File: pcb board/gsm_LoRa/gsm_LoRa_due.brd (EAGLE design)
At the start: 71.4 x 51.2 mm, 37 parts, among them IC1 TPS22810TDBVRQ1, IC3 DS3231MZ+, X1 22-23-2021

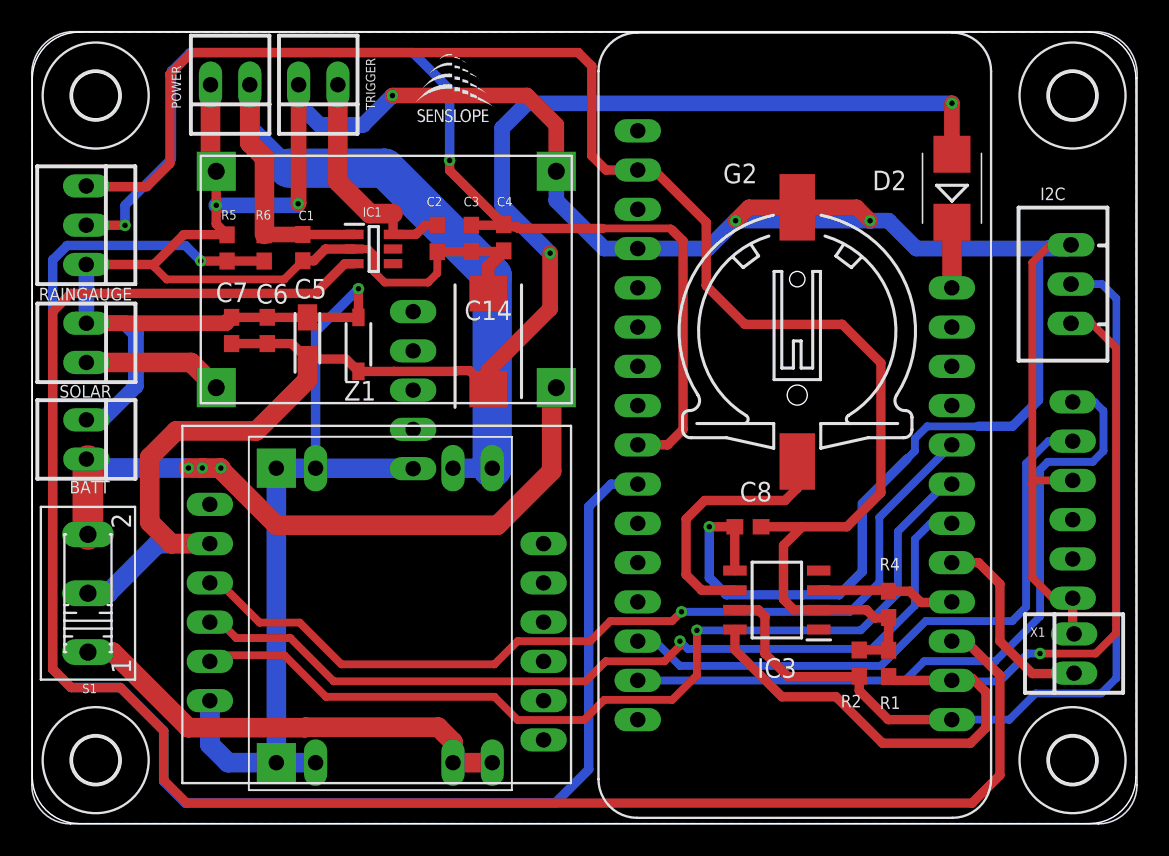
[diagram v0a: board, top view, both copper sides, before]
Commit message: added SPI connector
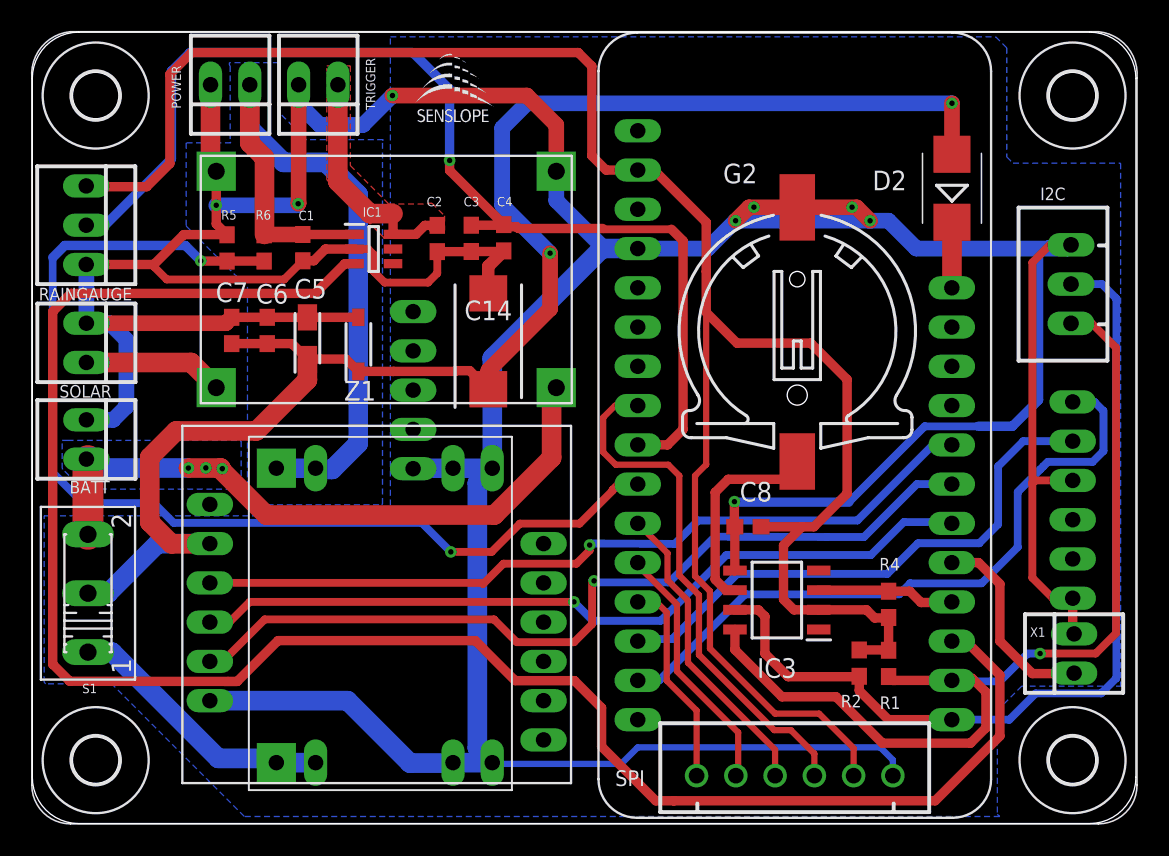
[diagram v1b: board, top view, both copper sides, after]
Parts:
- added SPI: JST-XH-06-PIN-ROUND-PAD, Rembrandt Electronics - JST XH Connectors v1-0:JST-XH-06-PACKAGE-ROUND-PAD
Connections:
- new net CS: SPI.4, U$1.P$8
- new net MISO: SPI.1, U$1.P$13
- new net MOSI: SPI.2, U$1.P$12
- new net SCK: SPI.3, U$1.P$11
- net +3V3: now also SPI.5
- net 12VIN: now also U$10.+IN, U$10.+IN1; no longer U$10.-IN, U$10.-IN1
- net DC-DC: now also U$10.+OUT, U$10.+OUT1; no longer U$10.-OUT, U$10.-OUT1
- net GND: now also SPI.6, U$10.-IN, U$10.-IN1, U$10.-OUT, U$10.-OUT1; no longer U$10.+IN, U$10.+IN1, U$10.+OUT, U$10.+OUT1
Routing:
- net +3V3: track 106.1 -> 141.0 mm
- net CS: track 0.00 -> 34.0 mm
- net N$5: track 102.8 -> 70.2 mm, vias 1 -> 2
- net GND: track 300.3 -> 328.2 mm, vias 7 -> 8
- net SCK: track 0.00 -> 20.0 mm
- net MOSI: track 0.00 -> 16.5 mm
- net MISO: track 0.00 -> 13.5 mm
- net DC-DC: track 29.9 -> 17.7 mm
- net GSM_RST: track 58.5 -> 52.0 mm
- net TXD_GSM: track 56.9 -> 51.7 mm
- net RX1: track 40.3 -> 35.7 mm
- net RXD_GSM: track 60.3 -> 55.7 mm
- net 12VIN: track 53.4 -> 49.7 mm
- net TX1: track 46.7 -> 43.2 mm
- net N$2: track 16.9 -> 14.0 mm
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- added copper zone on layer 16, net 12VIN
- added copper zone on layer 16, net BATT
- added copper zone on layer 1, net N$8

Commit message: Updated names on traces
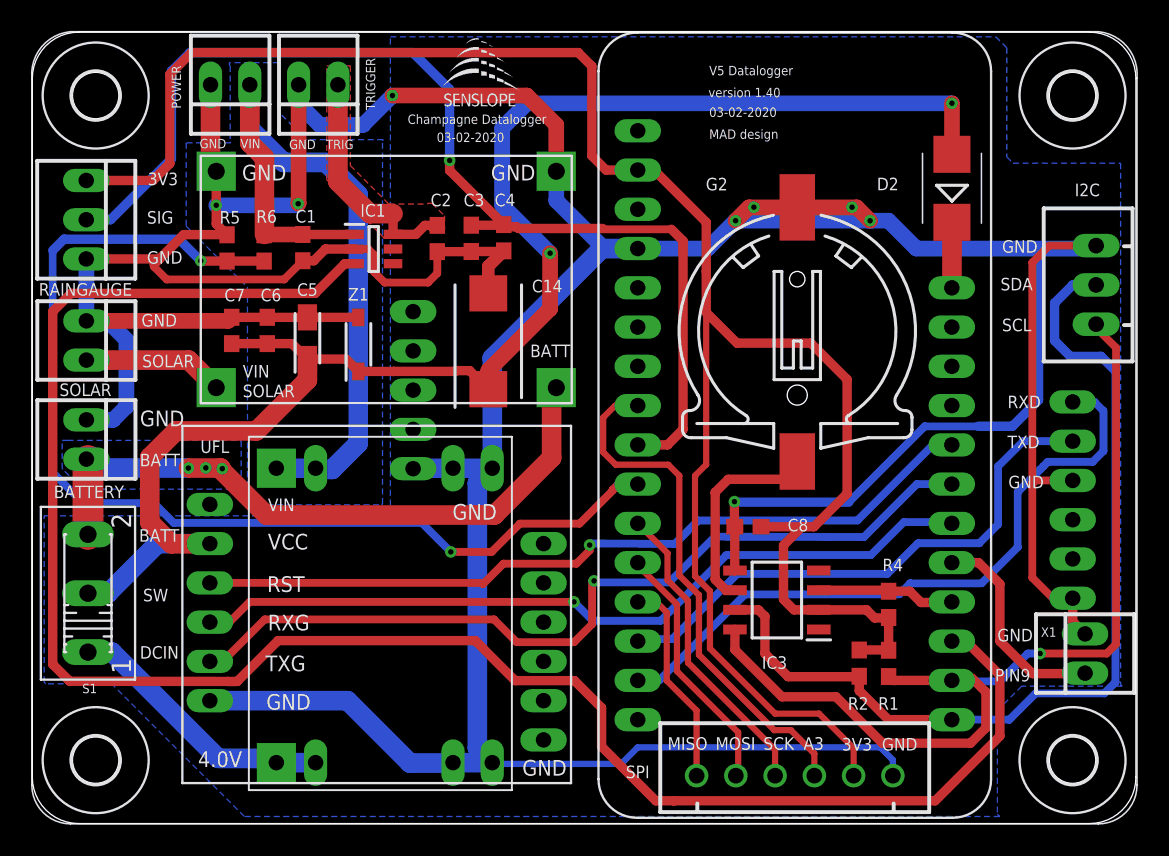
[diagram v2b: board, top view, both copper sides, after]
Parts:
- moved U$13 2.00 mm to (28.8, 47.9)
- moved I2C 1.63 mm to (68.8, 34.7)
- moved X1 0.71 mm to (68.1, 10.9)
- moved RAINGAUGE 0.36 mm to (3.49, 39.0)
- moved SOLAR 0.15 mm to (3.50, 31.2)
- renumbered BATT to BATTERY
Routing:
- net GND: track 328.2 -> 336.9 mm
- net SDA: track 58.6 -> 61.0 mm
- net SCL: track 63.6 -> 62.6 mm
- net PIN9: track 13.1 -> 13.8 mm
- net N$5: track 70.2 -> 70.8 mm
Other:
- board text added: "03-02-2020"
- board text added: "3V3"
- board text added: "4.0V"
- board text added: "A3"
- board text added: "BATT"
- board text added: "Champagne Datalogger"
- board text added: "DCIN"
- board text added: "GND"
- board text added: "MAD design"
- board text added: "MISO"
- board text added: "MOSI"
- board text added: "PIN9"
- board text added: "RST"
- board text added: "RXD"
- board text added: "RXG"
- board text added: "SCK"
- board text added: "SCL"
- board text added: "SDA"
- board text added: "SIG"
- board text added: "SOLAR"
- board text added: "SW"
- board text added: "TRIG"
- board text added: "TXD"
- board text added: "TXG"
- board text added: "UFL"
- board text added: "V5 Datalogger"
- board text added: "VCC"
- board text added: "VIN"
- board text added: "version 1.40"

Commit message: Added power IC switch for GSM Updated names of components
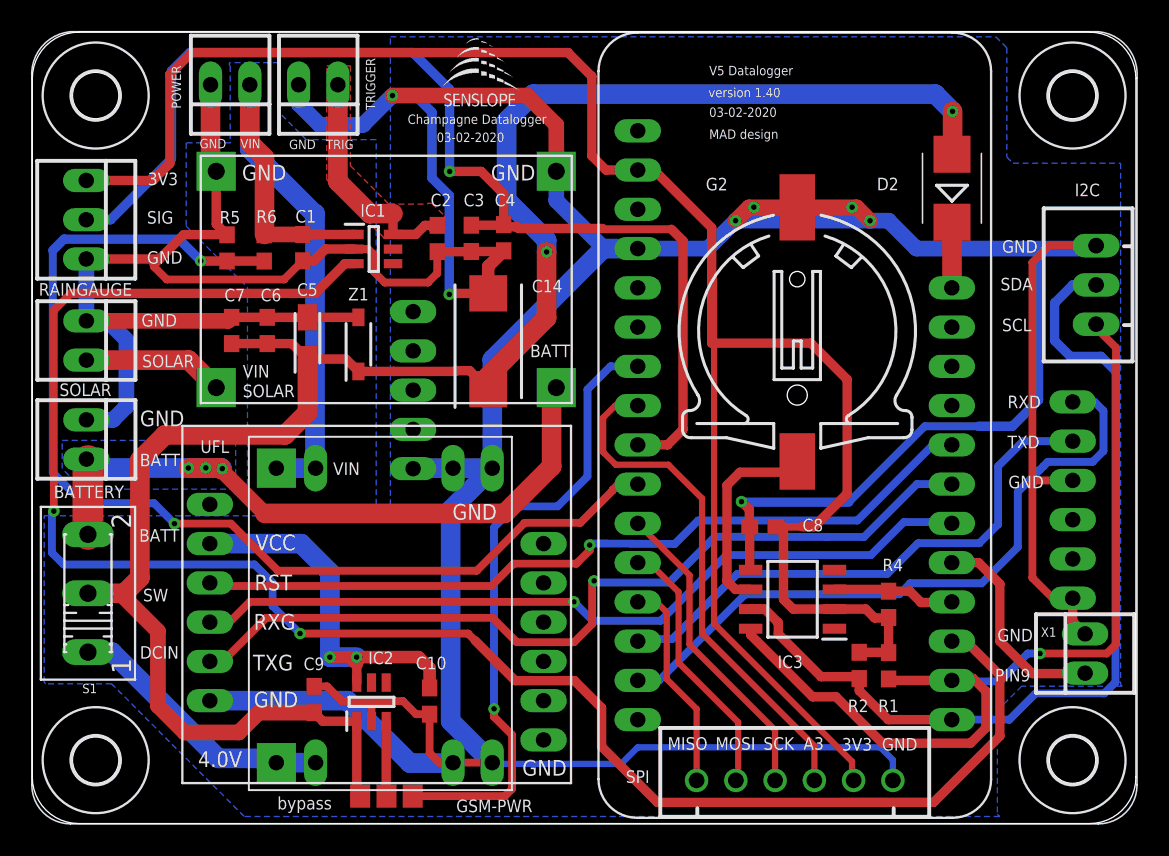
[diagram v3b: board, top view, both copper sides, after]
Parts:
- added C10, C9: (no value), eagle-ltspice:C0603
- added GSM-PWR: 0R-JUMPB, jump-0r-smd:B0R-JMP
- added IC2: TPS22810TDBVRQ1, TPS22810TDBVRQ1:SOT95P280X145-6N
- moved IC3 1.02 mm to (49.2, 14.4)
- moved C8 0.97 mm to (47.3, 19.1)
- moved SPI 0.30 mm to (49.3, 2.69)
- moved R1 0.15 mm to (55.4, 10.1)
- moved R2 0.15 mm to (53.5, 10.1)
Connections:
- new net GSMPWR: C10.1, IC2.6, U$9.VCC
- new net GSMSW: GSM-PWR.2, IC2.3
- new net GSM_PSW: GSM-PWR.3, U$1.P$7
- net 4V4: now also C9.2, GSM-PWR.1, IC2.1; no longer U$9.VCC
- net GND: now also C10.2, C9.1, IC2.2
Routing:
- net GSM_PSW: track 0.00 -> 40.9 mm, vias 0 -> 1
- net GSMPWR: track 0.00 -> 25.2 mm, vias 0 -> 2
- net 4V4: track 102.3 -> 127.3 mm
- net GND: track 336.9 -> 356.9 mm, vias 8 -> 7
- net DUETRIG: track 121.9 -> 116.5 mm, vias 0 -> 2
- net GSMSW: track 0.00 -> 4.85 mm
- net 12VIN: track 49.7 -> 45.1 mm
- net +3V3: track 140.8 -> 138.1 mm
- net BATT: track 42.8 -> 45.2 mm
- net SDA: track 61.0 -> 58.9 mm
- net SCL: track 62.6 -> 61.0 mm
- net RAIN: track 72.2 -> 73.4 mm
- net N$5: track 70.8 -> 71.8 mm
- net INTPIN6: track 8.95 -> 7.96 mm
- net MOSI: track 16.5 -> 17.3 mm
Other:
- board text added: "bypass"
